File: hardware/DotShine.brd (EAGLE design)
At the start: 30 x 65 mm, 55 parts, among them CN1 1X4-BIG, IC1 CAT24M010TS, IC3 SI1145, J3 USB-MICROB, U1 ATMEGA328P-MU-QFN32, U2 TMP102, U3 ATSHA204-TSU, X2 MC-RTC-RV-4162-C7-I2C, X3 S4B-ZR

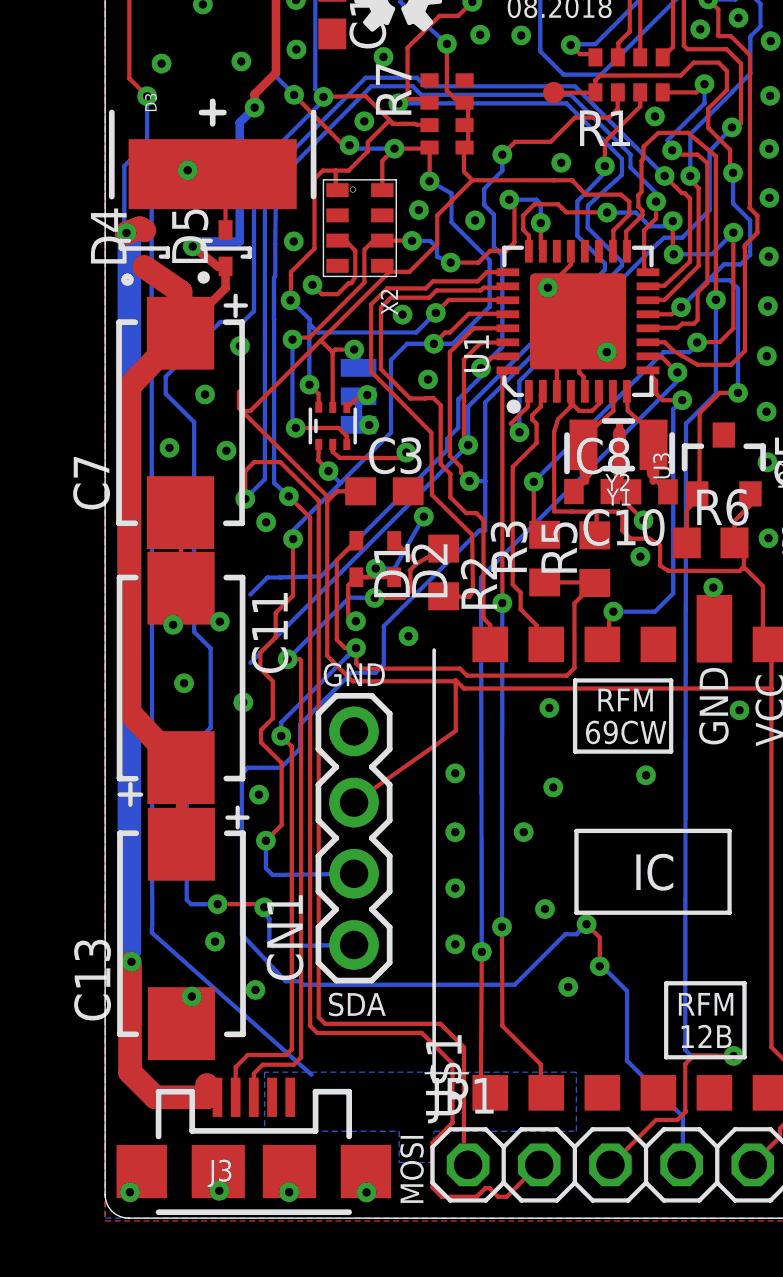
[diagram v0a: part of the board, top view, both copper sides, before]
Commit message: Remove IXYS SLMD121H9L solar cell 45mA@4.5V, use small cell and i2c micro crystal
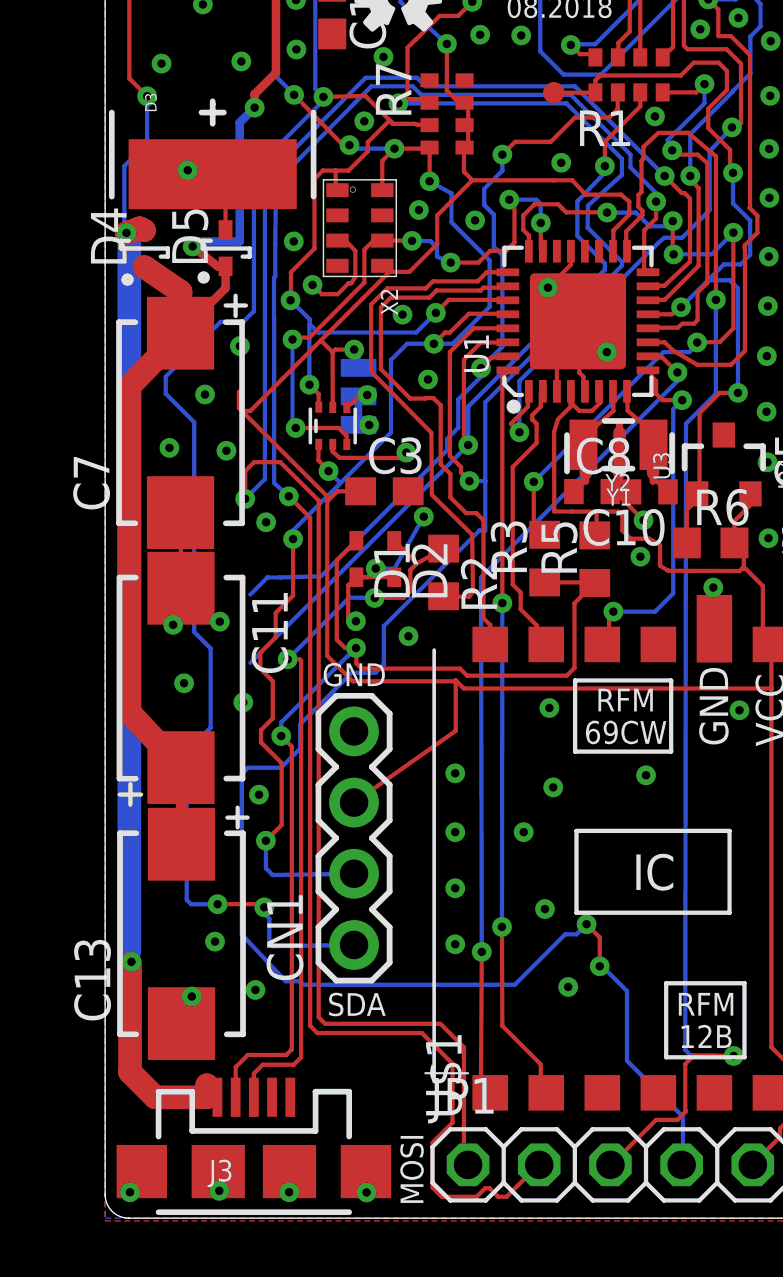
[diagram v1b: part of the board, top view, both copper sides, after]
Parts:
- R4: value 150Ω -> 330Ω
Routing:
- net SOLAR_OUT: track 39.3 -> 3.13 mm
- removed copper zone on layer 16, net SOLAR_OUT

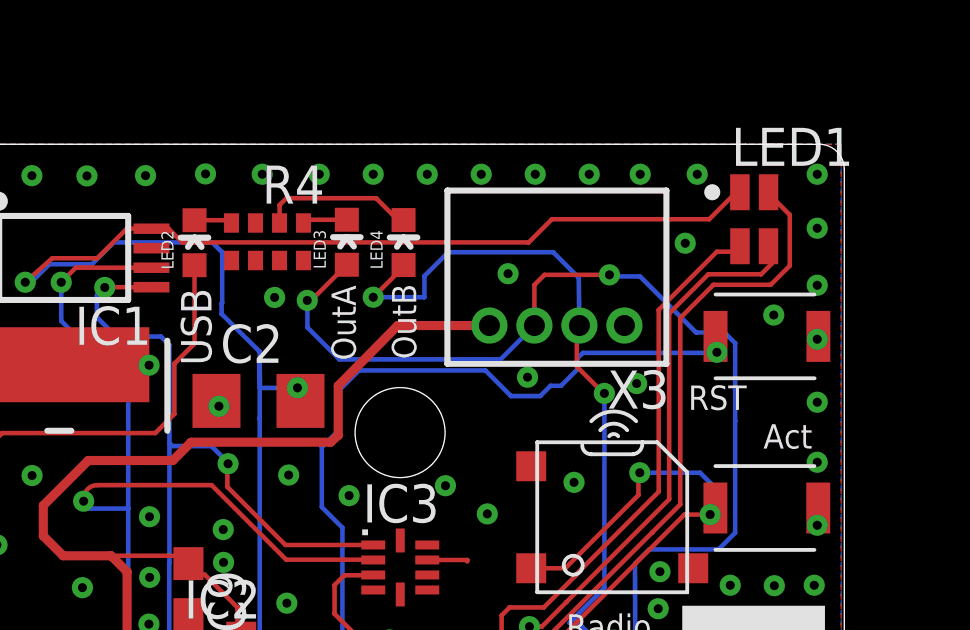
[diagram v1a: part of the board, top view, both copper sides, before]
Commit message: Add RST led
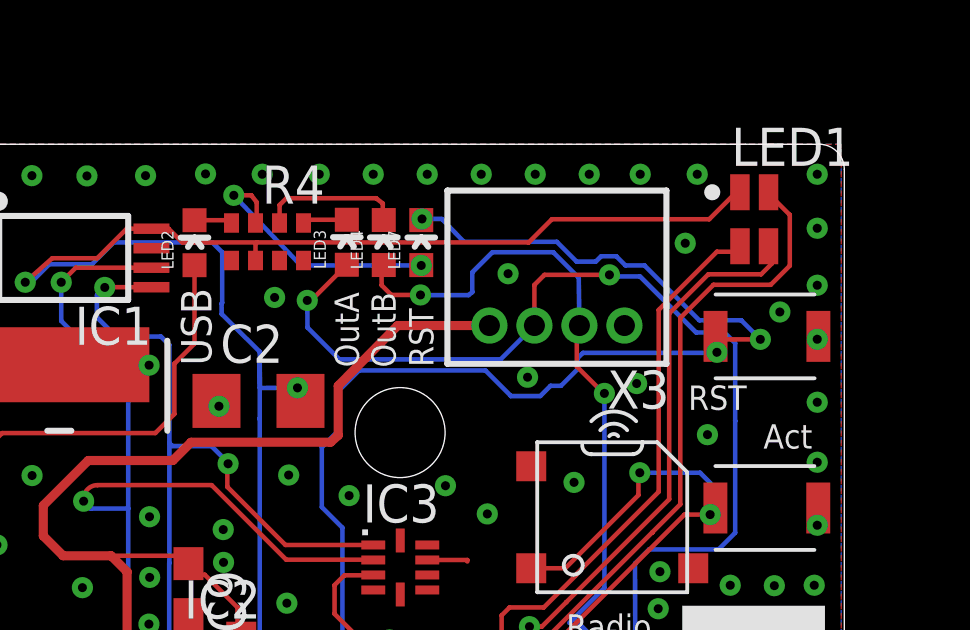
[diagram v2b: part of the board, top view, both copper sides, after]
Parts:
- added LED7: (no value), SparkFun:LED-0603
- moved LED4 0.66 mm to (14.7, 61.7)
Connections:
- net +3V3: now also R4.6
- net GND: no longer R4.6
- net N$10: now also LED7.A
- net RST: now also LED7.C
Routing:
- net RST: track 111.3 -> 126.0 mm, vias 6 -> 8
- net N$10: track 0.00 -> 9.01 mm, vias 0 -> 2
- net OUTB: track 47.3 -> 46.5 mm
- net +3V3: track 192.0 -> 192.6 mm
- net GND: vias 144 -> 145

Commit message: Add OG tag
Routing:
- net SCK: track 48.4 -> 47.0 mm
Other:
- board text removed: "Mihai Galos"

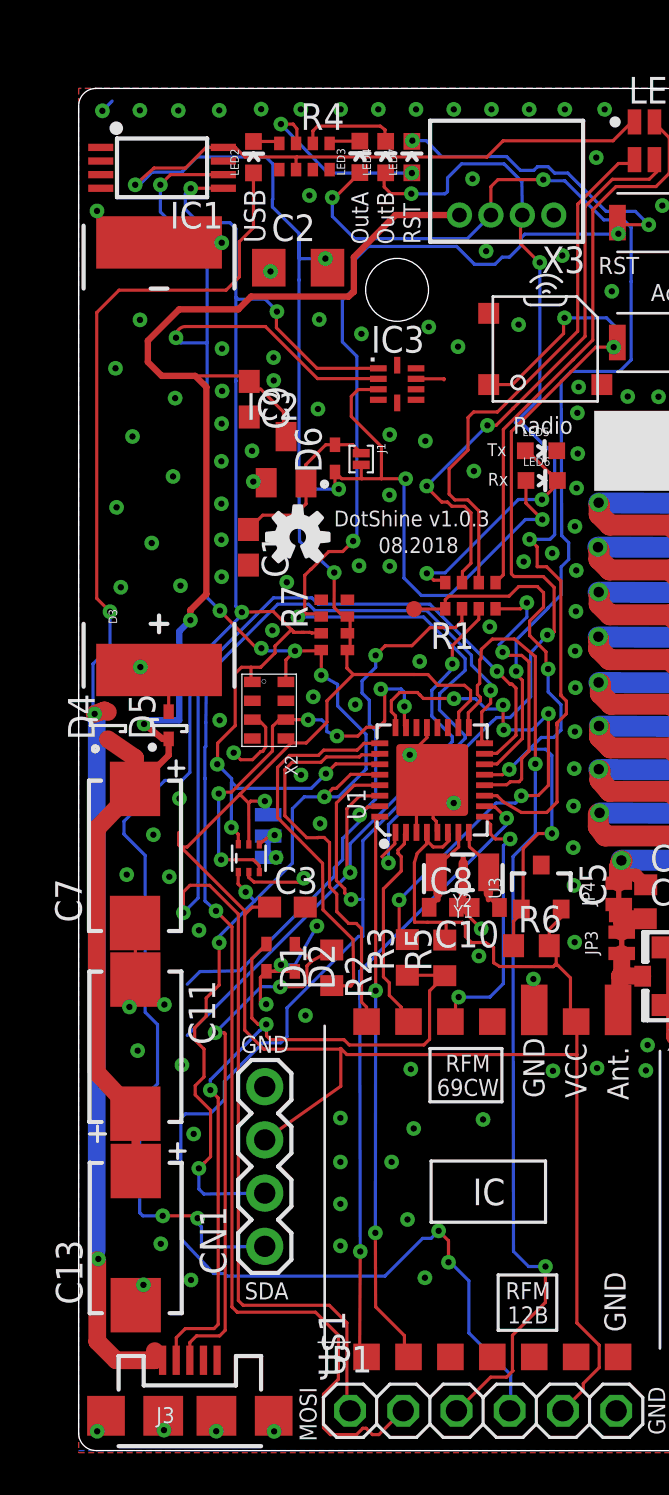
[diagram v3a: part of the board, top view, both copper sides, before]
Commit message: Invert cap, improve GND
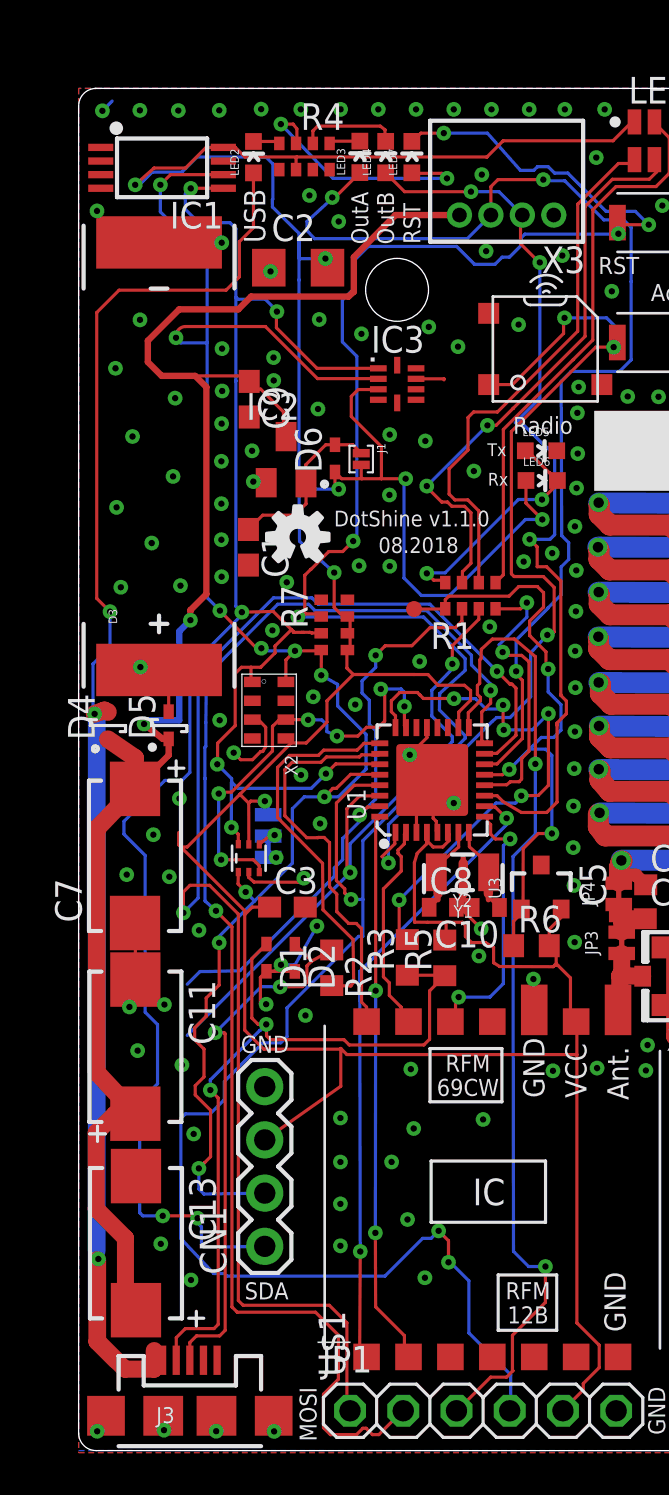
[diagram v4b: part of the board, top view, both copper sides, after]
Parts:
- D1, D2: value (none) -> 5V Zener
- moved C13 0.24 mm to (2.74, 9.90), turned to 270 degrees
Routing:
- net +5V: track 74.3 -> 83.1 mm
- net N$10: track 9.01 -> 12.4 mm
- net OUTB: track 46.5 -> 43.4 mm
- net OUTA: track 51.1 -> 53.2 mm
- net USB_FOR_LED: track 67.5 -> 68.5 mm
- net GND: track 40.0 -> 39.2 mm
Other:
- board text added: "DotShine v1.1.0"
- board text removed: "DotShine v1.0.3"

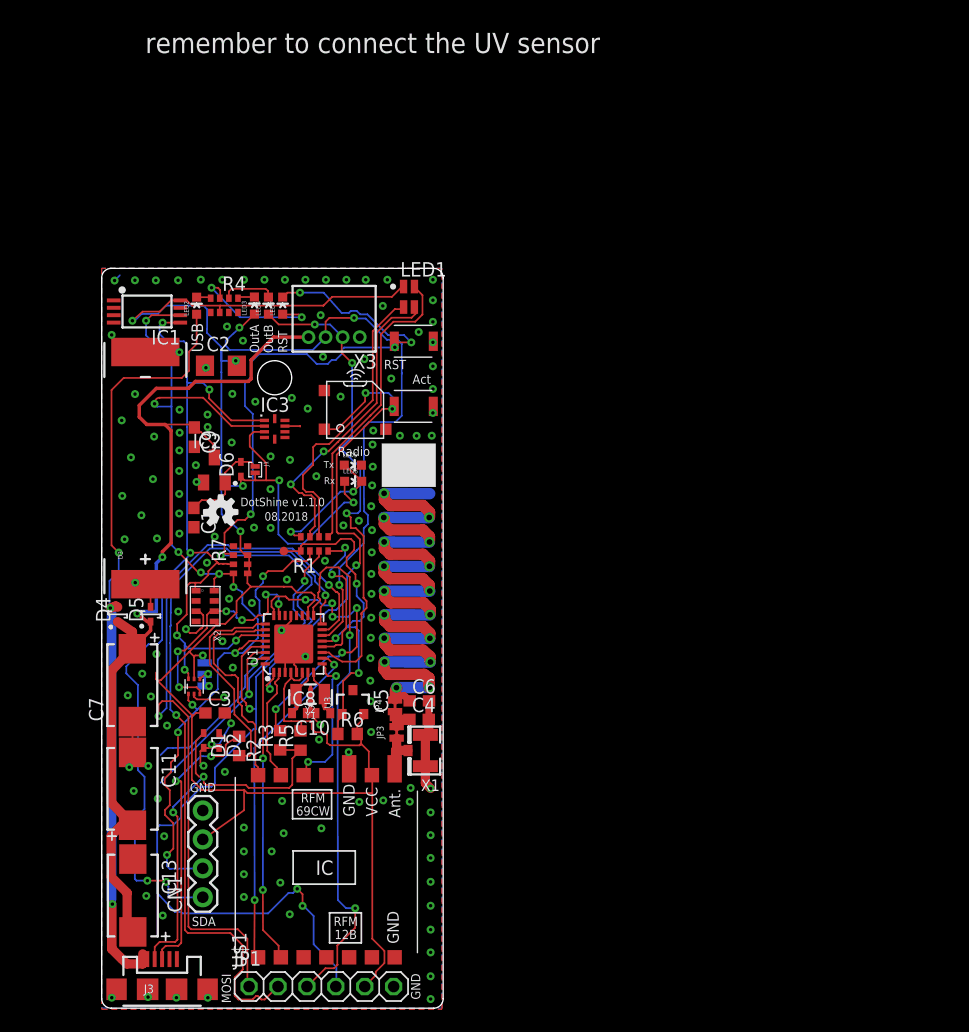
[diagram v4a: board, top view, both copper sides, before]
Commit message: Refactor Caps from 5V to 3.3V, update version
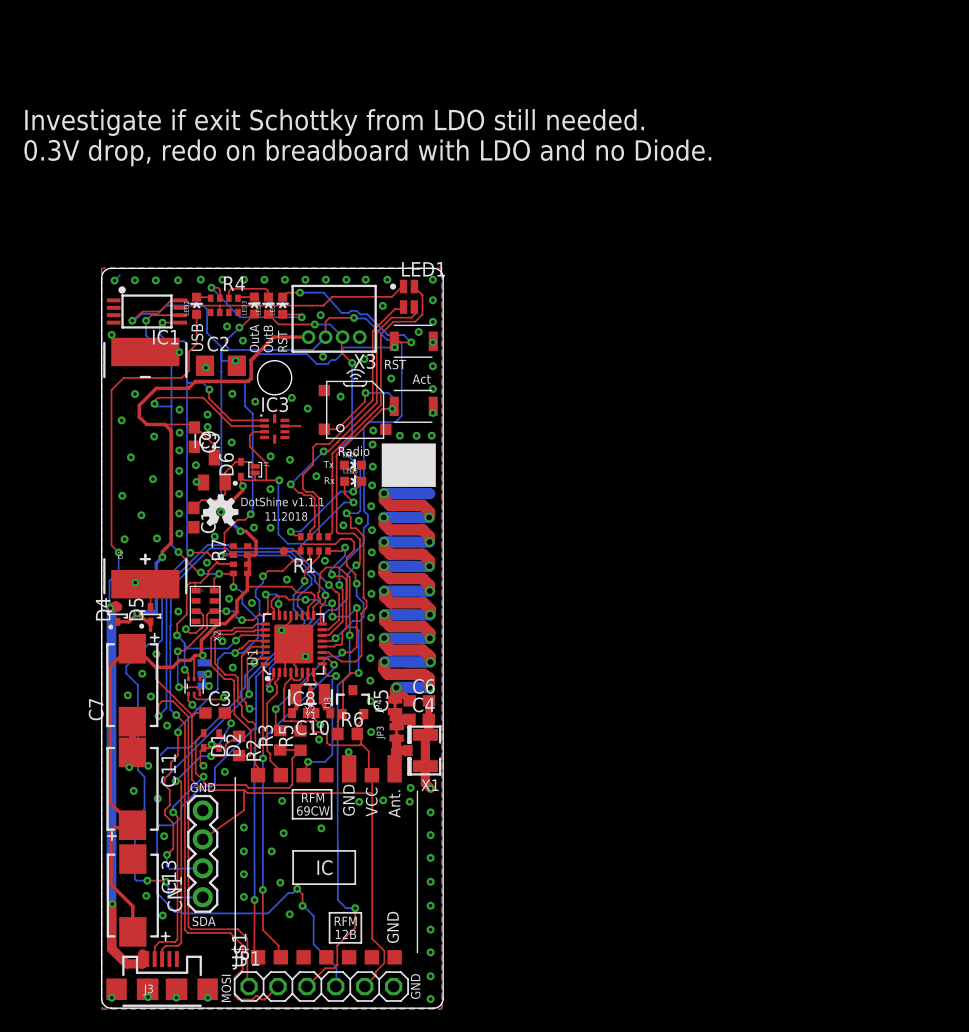
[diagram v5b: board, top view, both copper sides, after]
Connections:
- net +3V3: now also C11.+, C13.+, C7.+
- net +5V: no longer C11.+, C13.+, C7.+
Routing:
- net +3V3: track 192.6 -> 227.0 mm, vias 7 -> 8
- net +5V: track 83.1 -> 51.3 mm
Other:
- board text added: "11.2018"
- board text added: "DotShine v1.1.1"
- board text added: "Investigate if exit Schottky from LDO still needed. 0.3V drop, redo on breadboard with LDO and no Diode."
- board text removed: "08.2018"
- board text removed: "DotShine v1.1.0"
- board text removed: "remember to connect the UV sensor"

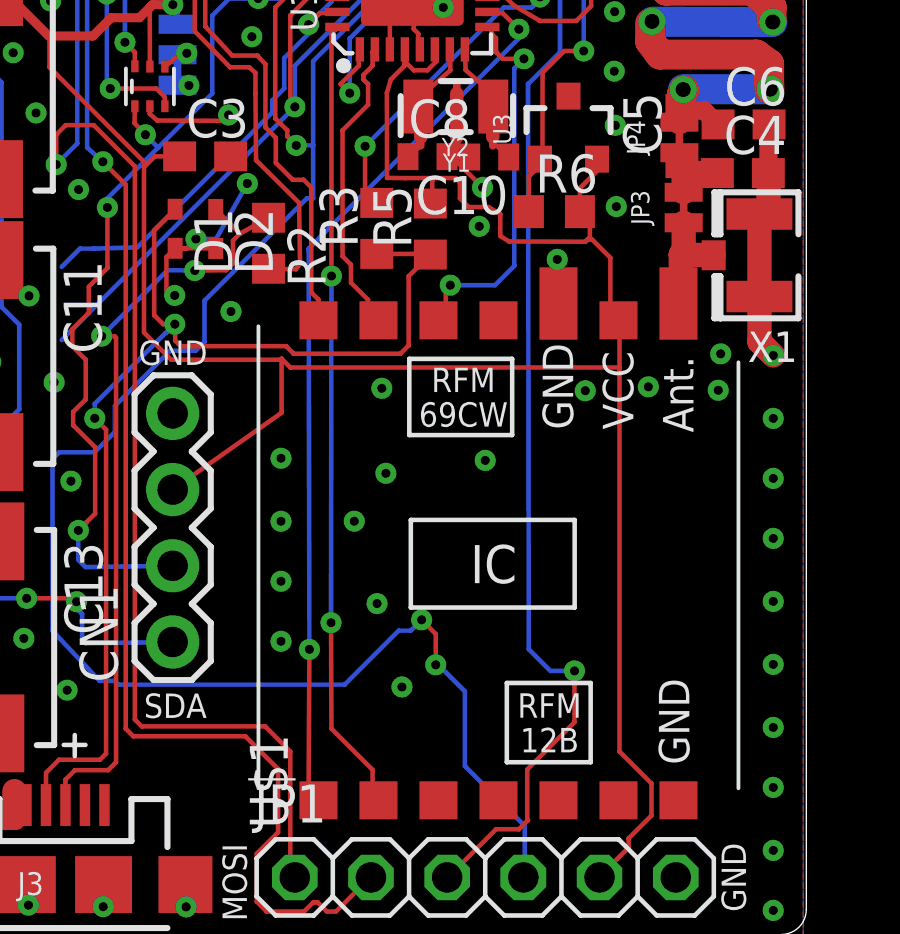
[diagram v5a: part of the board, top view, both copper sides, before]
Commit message: Add SJ for ADCENA and RST -> HW reset through SW
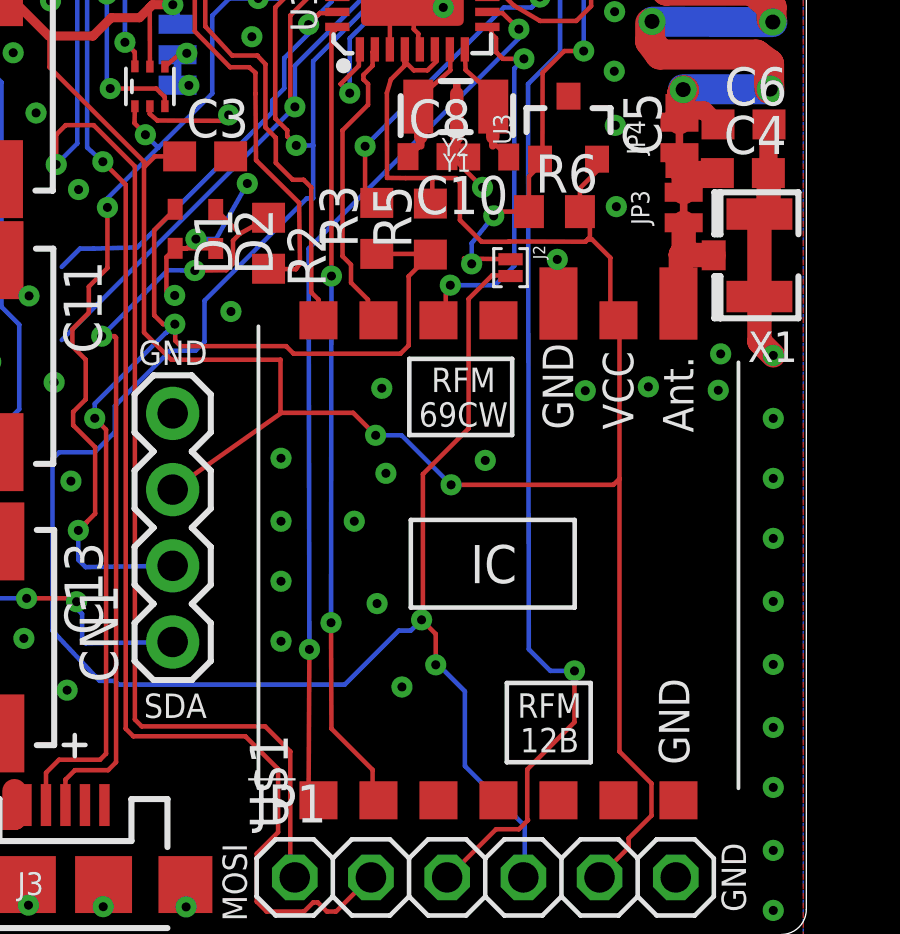
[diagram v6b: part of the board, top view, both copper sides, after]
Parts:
- added J2: (no value), solderjumper:2.MED
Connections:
- net ADCENA: now also J2.1
- net RST: now also J2.2
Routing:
- net RST: track 126.3 -> 139.4 mm
- net ADCENA: track 30.6 -> 35.5 mm, vias 3 -> 5
- net +3V3: track 227.0 -> 227.9 mm, vias 8 -> 10
- net GND: vias 145 -> 144
